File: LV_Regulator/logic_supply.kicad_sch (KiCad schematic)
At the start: 18 parts, among them U4 MCP1826T-ADJE_DC, U5 MCP1826T-ADJE_DC

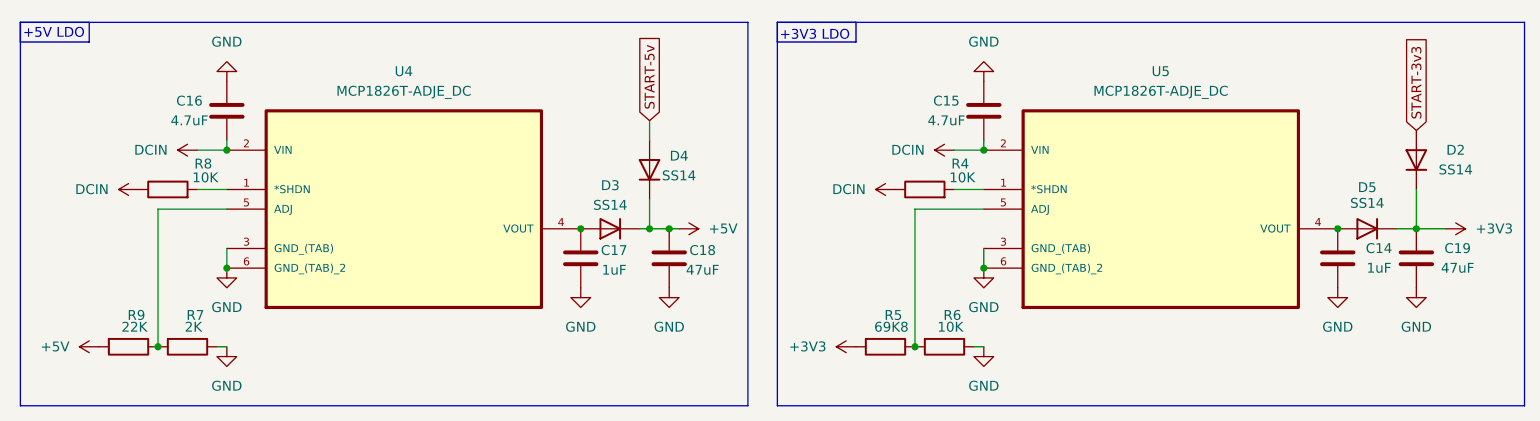
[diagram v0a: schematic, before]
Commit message: Added Start Control
Added Start Control MCU to the LV_Kontrola_Main, added hsc/lsc to LV_Regulator, fixed component numbering
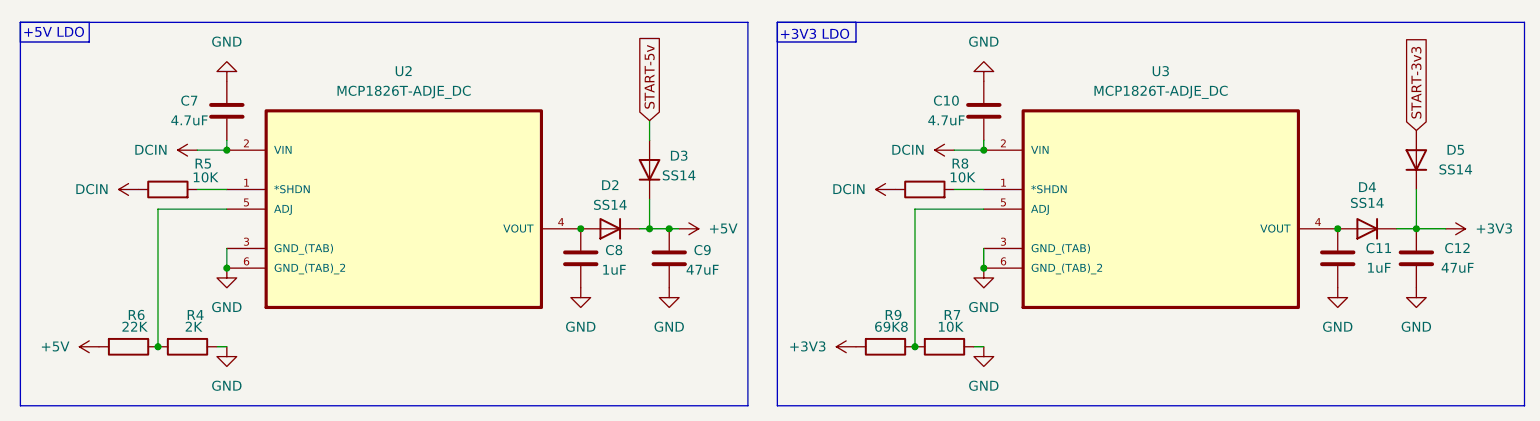
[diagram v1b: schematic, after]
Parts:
- renumbered C15 to C10, C14 to C11, C19 to C12, C16 to C7, C17 to C8, C18 to C9, D3 to D2, D4 to D3, D5 to D4, D2 to D5, R7 to R4, R8 to R5, R9 to R6, R6 to R7, R4 to R8, R5 to R9, U4 to U2, U5 to U3

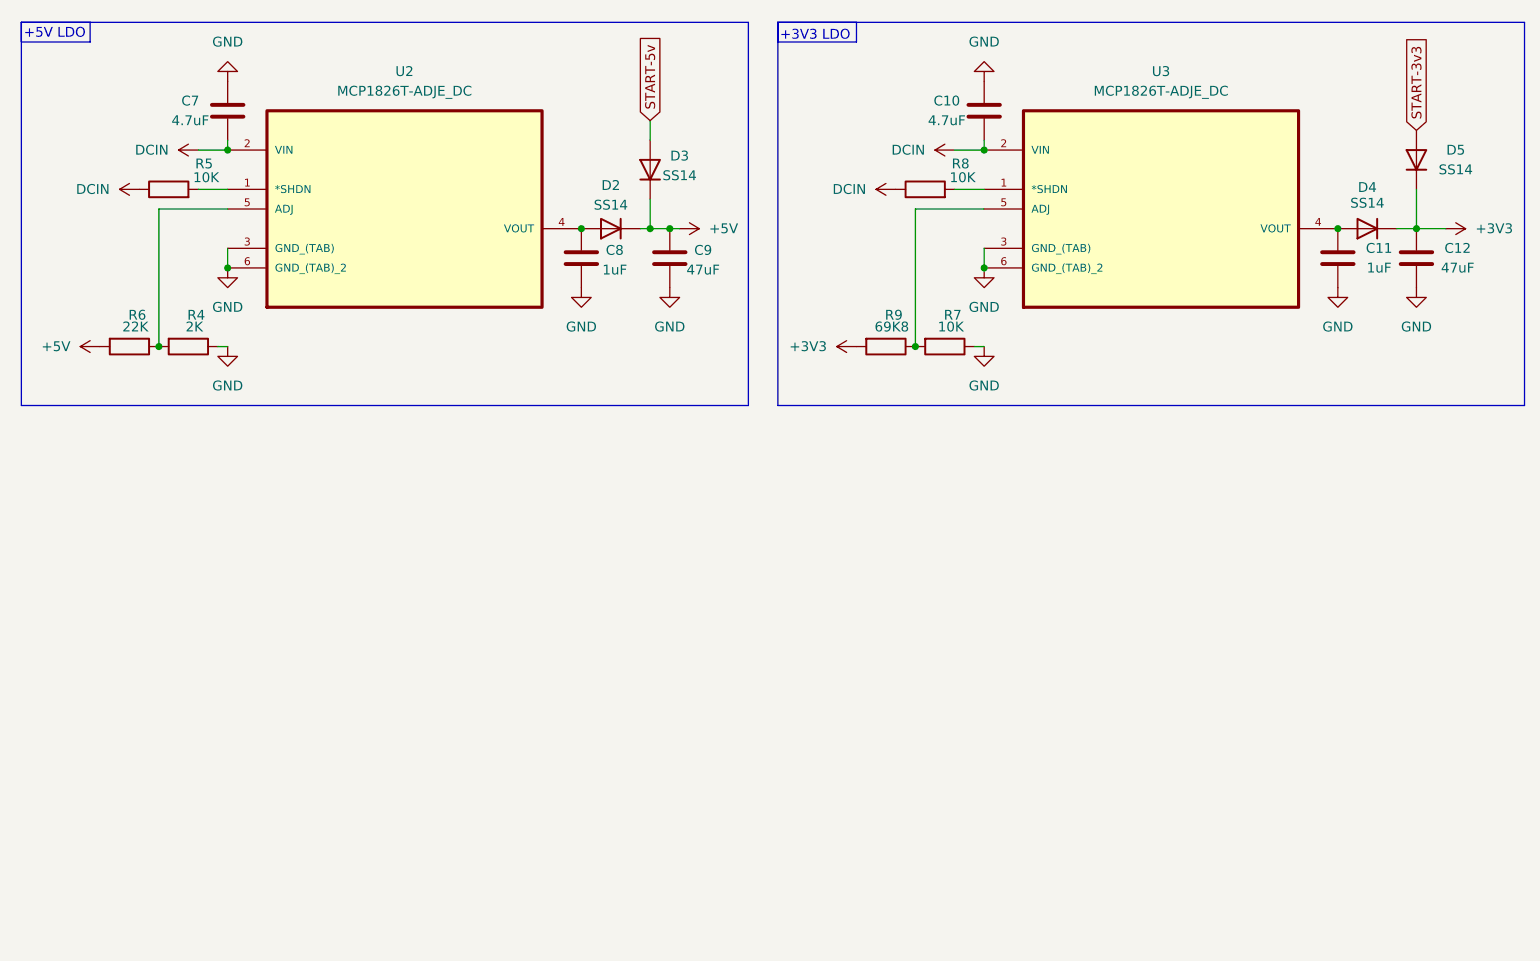
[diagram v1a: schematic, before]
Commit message: Added Stat logic
Added start mcu and associated components to the LV_Kontrola_Main schematic, added STM32CubeIDE project and basic configuration, added fuses to LV_Regulator
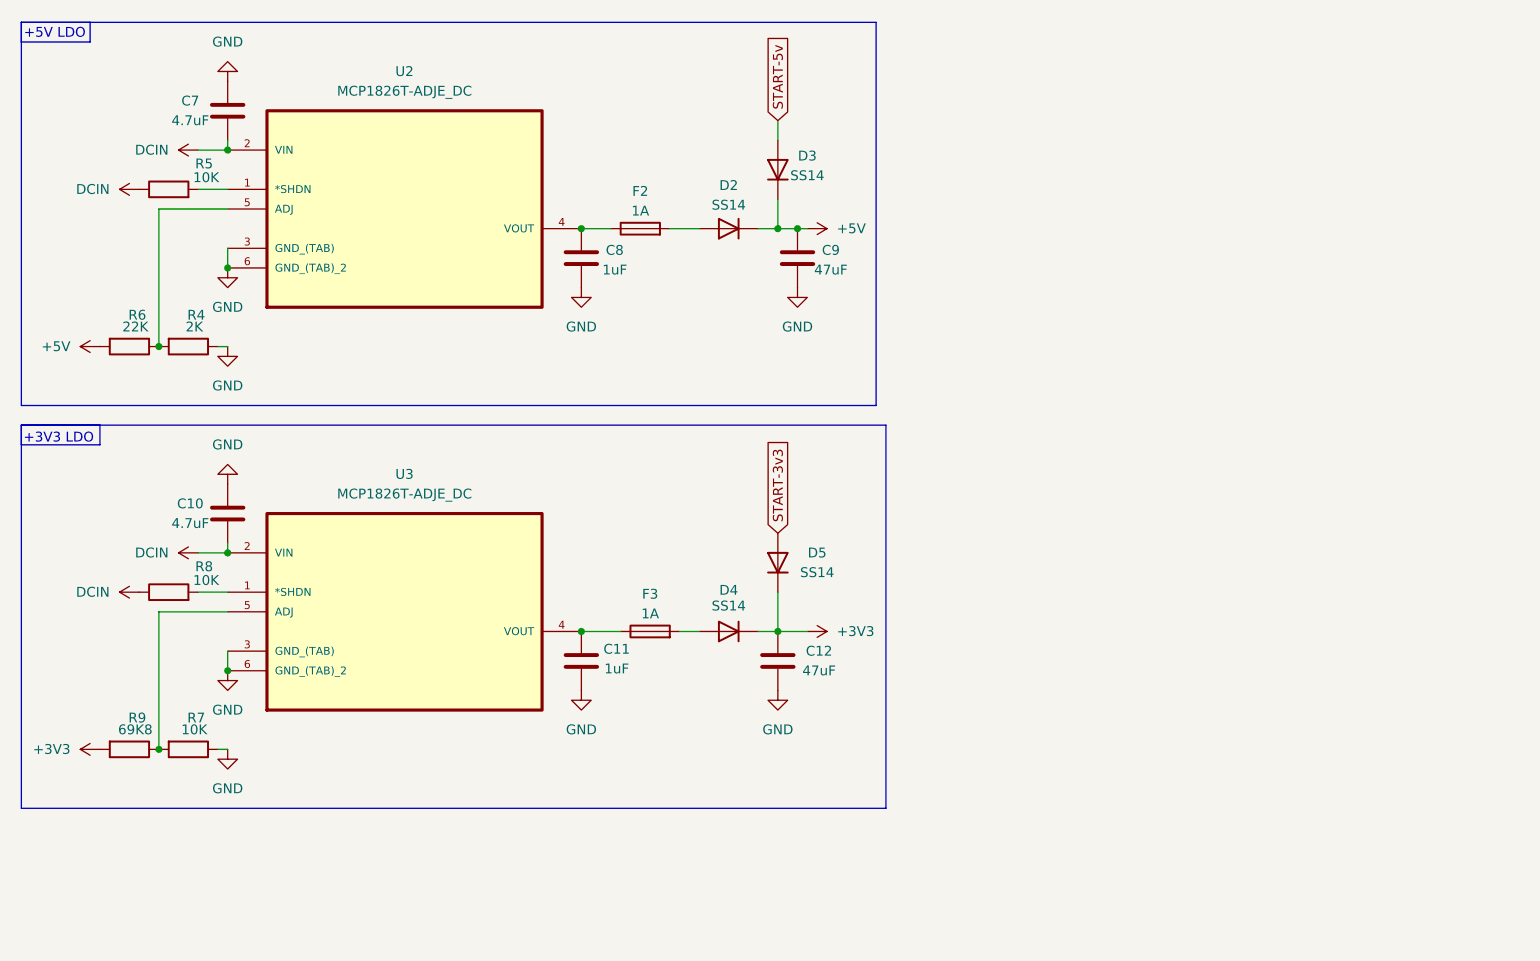
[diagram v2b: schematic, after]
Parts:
- added F2, F3: 1A, symbol Device:Fuse
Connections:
- net at C11.2, U3.4 (VOUT): now also F3.1; no longer D4.2 (A)
- net at C8.2, U2.4 (VOUT): now also F2.1; no longer D2.2 (A)
- new net: D4.2 (A), F3.2
- new net: D2.2 (A), F2.2
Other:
- moved on the sheet: C10, C11, C12, C9, D2, D3, D4, D5, R7, R8, R9, U3

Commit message: LV_Regulator Control changes
Added debug and development equipment, added config. eeprom, more...
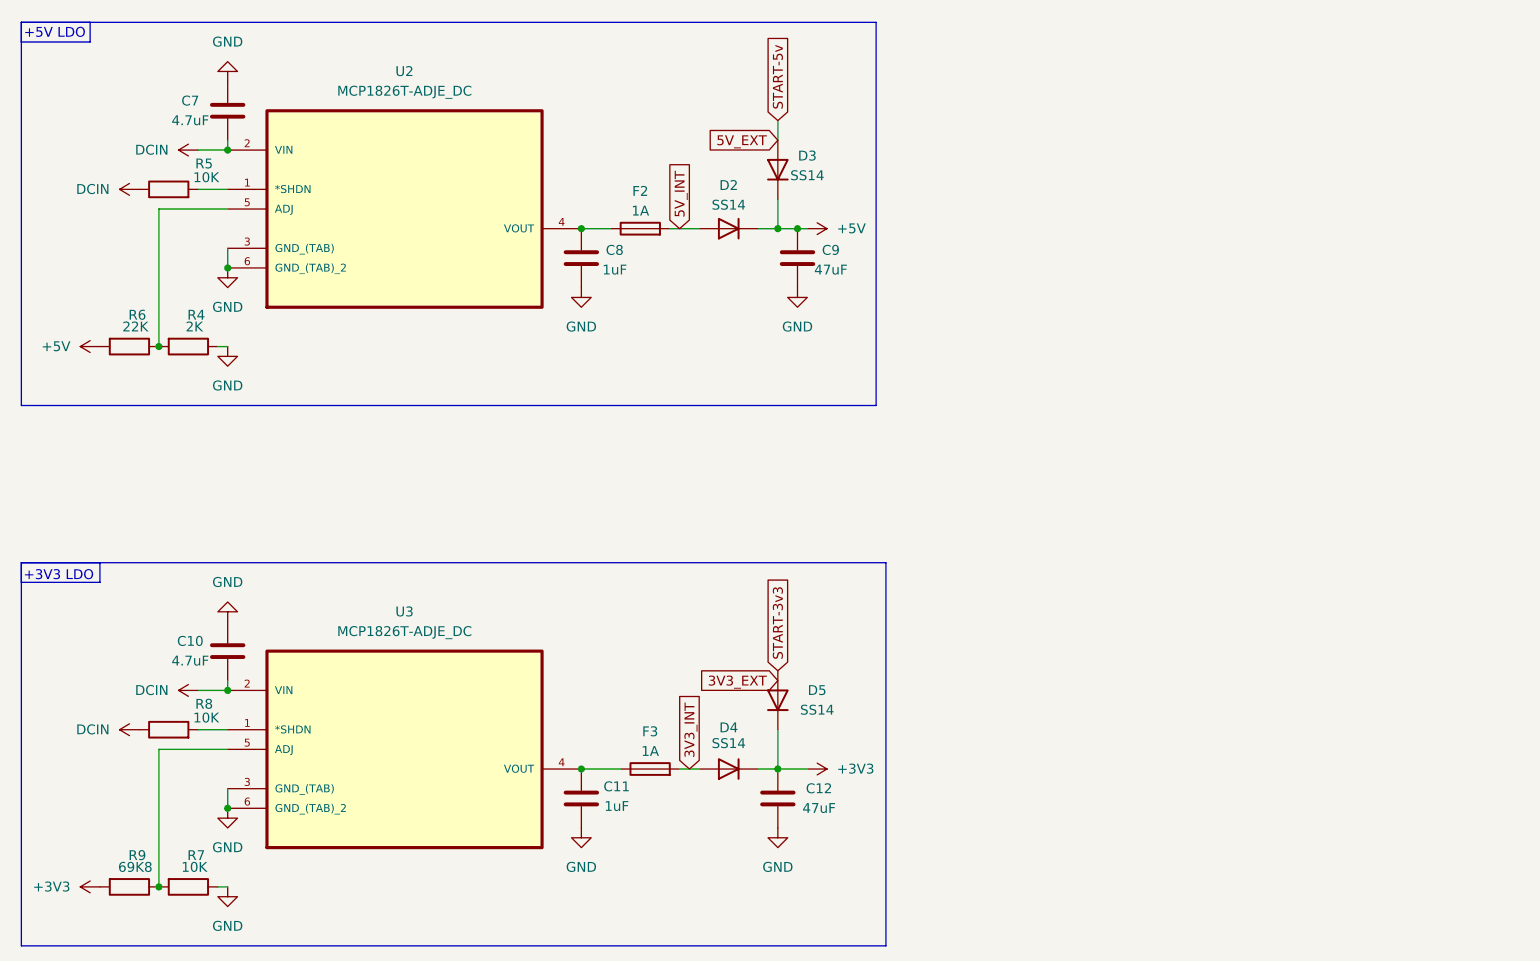
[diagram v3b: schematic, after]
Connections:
- net 3V3_INT: now reaches D4.2 (A), F3.2
- net 5V_INT: now reaches D2.2 (A), F2.2
- net START-5v renamed 5V_EXT
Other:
- moved on the sheet: C10, C11, C12, D4, D5, F3, R7, R8, R9, U3

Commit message: Changes of PCB and Schematic files for the LV_Regulator
Removed old LDOs, added new LDOs, defined initial pcb size and I/O ports
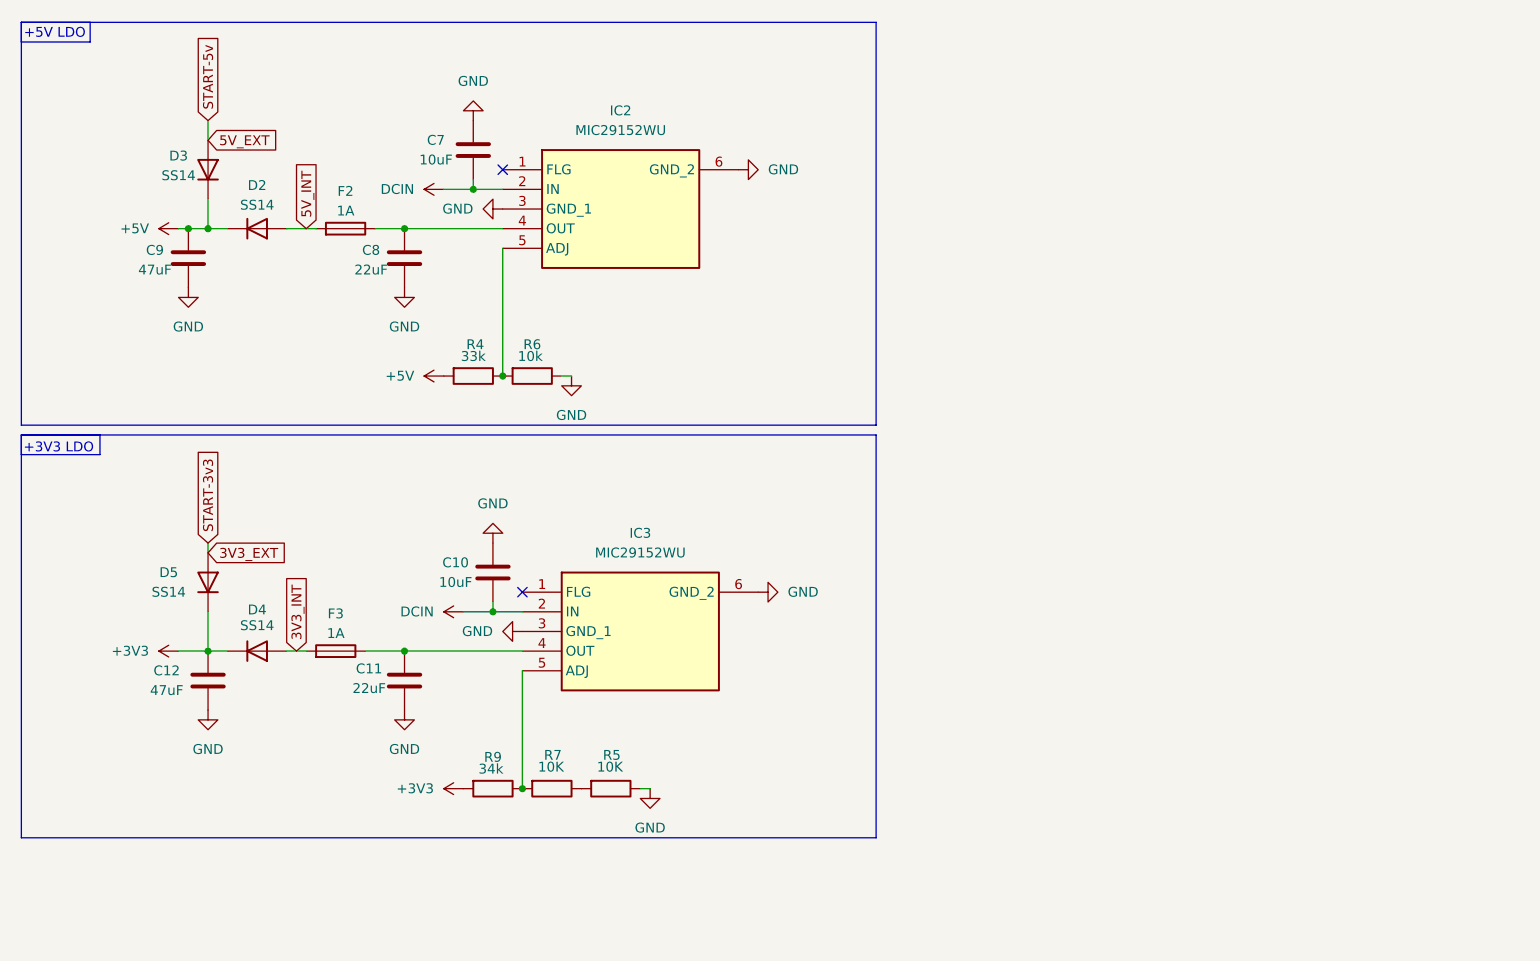
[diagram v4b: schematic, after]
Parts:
- removed R8: 10K, symbol Device:R
- removed U2, U3: MCP1826T-ADJE_DC, MCP1826T-ADJE_DC:SOT230P700X180-6N, symbol MCP1826T-ADJE_DC:MCP1826T-ADJE_DC
- added IC2, IC3: MIC29152WU, MIC29152WU, symbol MIC29152WU:MIC29152WU
- C10, C7: value 4.7uF -> 10uF
- C11, C8: value 1uF -> 22uF
- R4: value 2K -> 33k
- R6: value 22K -> 10k
- R9: value 69K8 -> 34k
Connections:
- net START-3v3 is gone; now on net 3V3_EXT: D5.2 (A)
- net +3V3: now also R9.2; no longer R7.2
- net DCIN: now also IC2.2 (IN), IC3.2 (IN); no longer R5.1
- net GND: now also R5.1, IC2.3 (GND_1), IC2.6 (GND_2), IC3.3 (GND_1), IC3.6 (GND_2); no longer R9.1
- net at R7.1: now also R5.2; no longer R9.2
- net at R4.1, R6.2: now also IC2.5 (ADJ)
- net at C8.2, F2.1: now also IC2.4 (OUT)
- net at C11.2, F3.1: now also IC3.4 (OUT)
- new net: IC3.5 (ADJ), R7.2, R9.1
- no-connect marks 0 -> 2
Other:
- moved on the sheet: C10, C11, C12, C7, C8, C9, D2, D3, D4, D5, F2, F3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

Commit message: Added footprints and Test points
Added test points, yet to connect them have to find where they all go exactly
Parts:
- R4, R5, R6, R7, R9: footprint (none) -> Resistor_SMD:R_1206_3216Metric_Pad1.30x1.75mm_HandSolder
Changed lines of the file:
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@@
 			)
 		)
-		(property "Footprint" ""
+		(property "Footprint" "Resistor_SMD:R_1206_3216Metric_Pad1.30x1.75mm_HandSolder"
 			(at 81.28 117.602 90)
 			(effects
@@
 			)
 		)
-		(property "Footprint" ""
+		(property "Footprint" "Resistor_SMD:R_1206_3216Metric_Pad1.30x1.75mm_HandSolder"
 			(at 78.74 64.262 90)
 			(effects
@@
 			)
 		)
-		(property "Footprint" ""
+		(property "Footprint" "Resistor_SMD:R_1206_3216Metric_Pad1.30x1.75mm_HandSolder"
 			(at 88.9 117.602 90)
 			(effects
@@
 			)
 		)
-		(property "Footprint" ""
+		(property "Footprint" "Resistor_SMD:R_1206_3216Metric_Pad1.30x1.75mm_HandSolder"
 			(at 86.36 64.262 90)
 			(effects
@@
 			)
 		)
-		(property "Footprint" ""
+		(property "Footprint" "Resistor_SMD:R_1206_3216Metric_Pad1.30x1.75mm_HandSolder"
 			(at 96.52 117.602 90)
 			(effects
